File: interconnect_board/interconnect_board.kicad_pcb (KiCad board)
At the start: 2 copper layers, 77.5 x 96.5 mm, 45 parts, among them P1 CONN_02X10, P2 CONN_02X07, P3 CONN_01X06, P4 CONN_01X10, P5 CONN_01X08, P6 CONN_01X02, P7 CONN_01X02, P8 CONN_01X02, P9 CONN_01X02

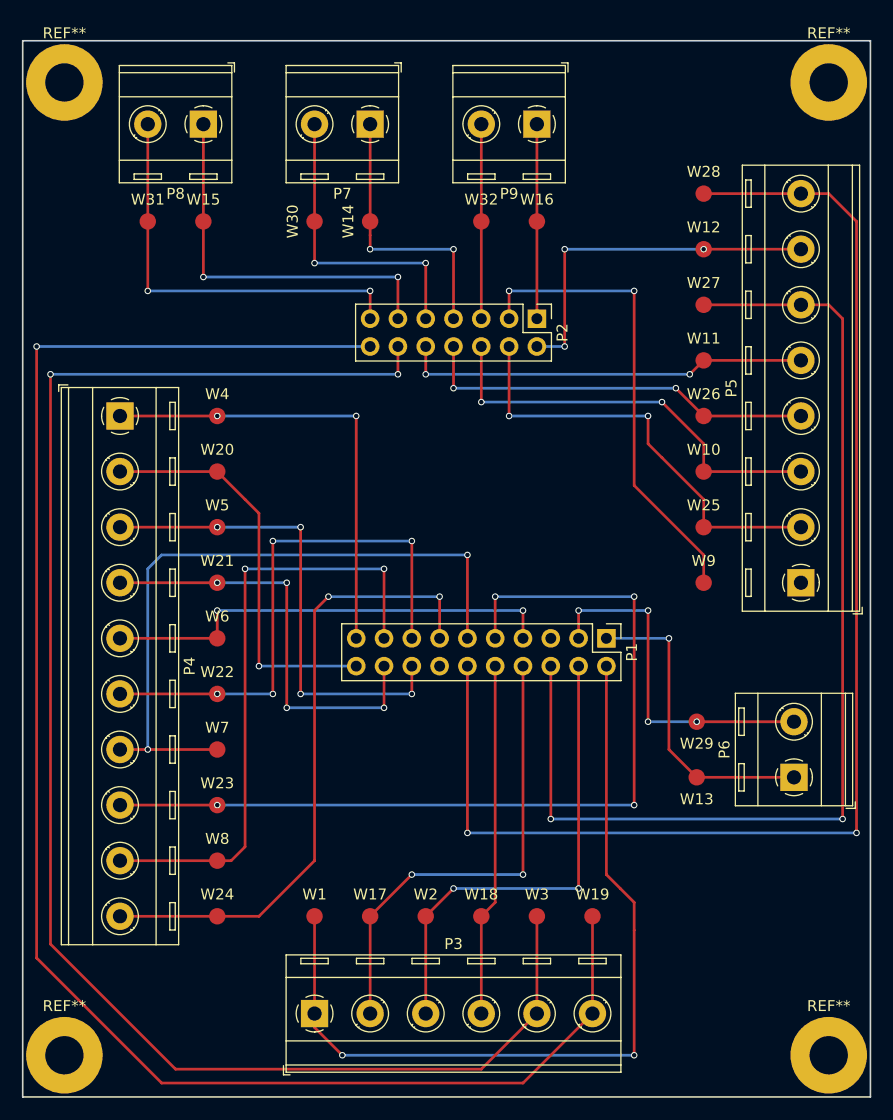
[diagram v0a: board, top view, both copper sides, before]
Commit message: Placed component labels on interconnect board
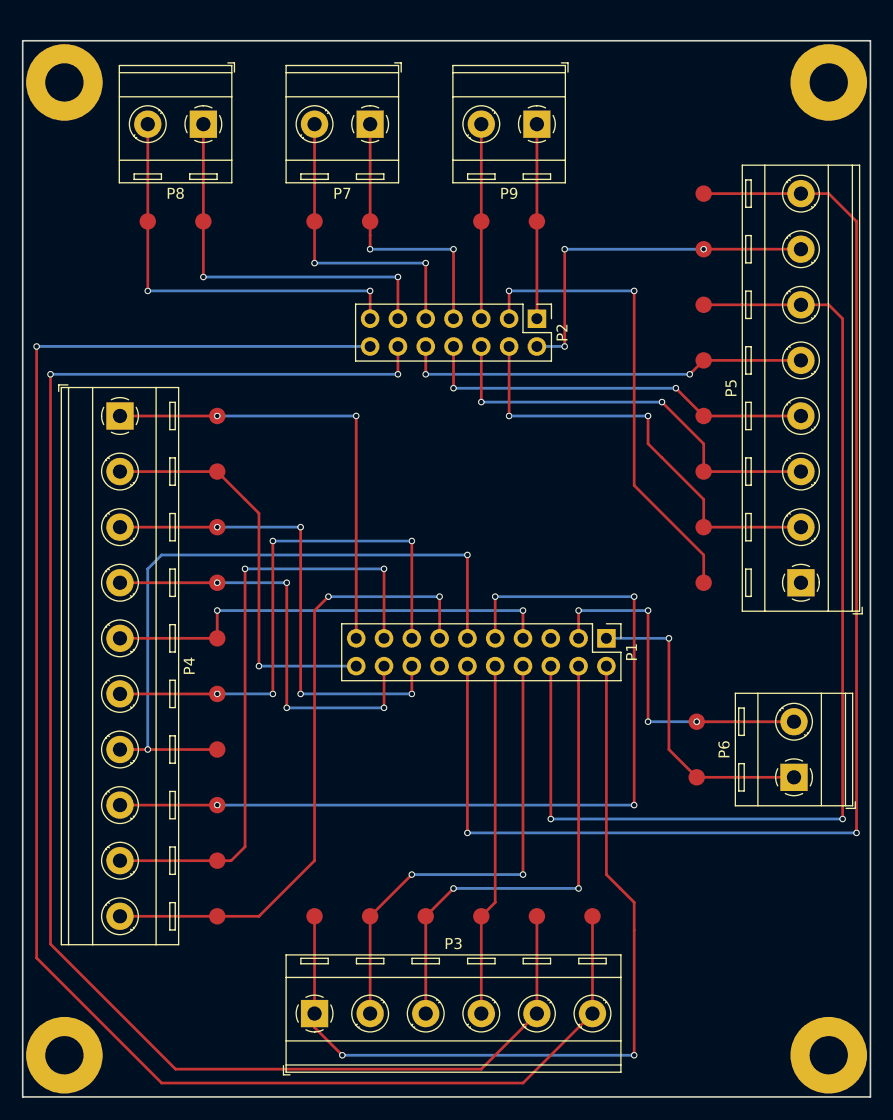
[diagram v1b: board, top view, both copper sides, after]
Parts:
- W1: value HVPL_1_P -> HVPL_1
- W10: value Drive_BTN_+5_P -> Drive_BTN_+5
- W11: value Drive_LED_P -> Drive_LED
- W12: value CC_LED_P -> CC_LED
- W13: value CAN_H_P -> CAN_H
- W14: value AIRs+_P -> AIRs+
- W15: value IMD_Status_P -> IMD_Status
- W16: value CH_GND_P -> CH_GND
- W17, W2: value HVPL_1_RTN_P -> HVPL_1_RTN
- W18: value HVPL_2_RTN_P -> HVPL_2_RTN
- W19: value RTDS_RTN_P -> RTDS_RTN
- W20: value Brake_24B_P -> Brake_24B
- W21: value BOT_P -> BOT
- W22: value APPS1_P -> APPS1
- W23: value APPS2_5_P -> APPS2_5
- W24: value RTN_GLV_P -> RTN_GLV
- W25: value IMD_Fault_LED_P -> IMD_Fault_LED
- W26: value Drive_BTN_P -> Drive_BTN
- W27: value HVPL_Cock_P -> HVPL_Cock
- W28: value HVPL_Cock_RTN_P -> HVPL_Cock_RTN
- W29: value CAN_L_P -> CAN_L
- W3: value RTDS_P -> RTDS
- W30: value AIRs-_P -> AIRs-
- W31: value IMD_PWM_P -> IMD_PWM
- W32: value 24LV_P -> 24LV
- W4: value Brake_24A_P -> Brake_24A
- W5: value BP_P -> BP
- W6: value APPS1_10_P -> APPS1_10
- W7: value APPS1_RTN_P -> APPS1_RTN
- W8: value APPS2_P -> APPS2
- W9: value LV_RTN_P -> LV_RTN
